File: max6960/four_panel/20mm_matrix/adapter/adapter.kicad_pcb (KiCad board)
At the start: 2 copper layers, 40 x 40 mm, 6 parts, among them M1 BETLUX-LED-8X8_C, M2 BETLUX-LED-8X8_C, M3 BETLUX-LED-8X8_C, M4 BETLUX-LED-8X8_C, P1 LED-MATRIX-2X-8X8-FEMALE, P2 LED-MATRIX-2X-8X8-FEMALE

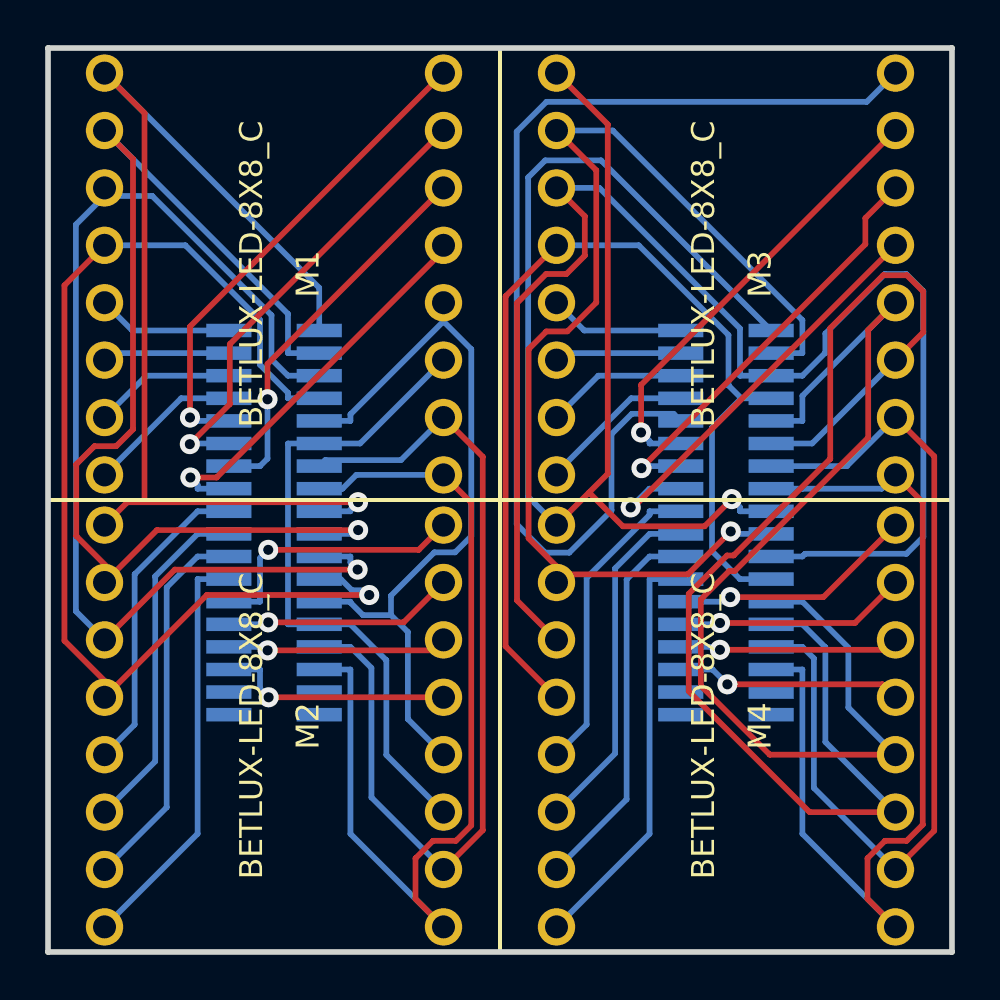
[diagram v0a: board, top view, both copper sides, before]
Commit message: Re-routed four matrix panel driver and adapter. Switched to board-to-board connectors from major league.
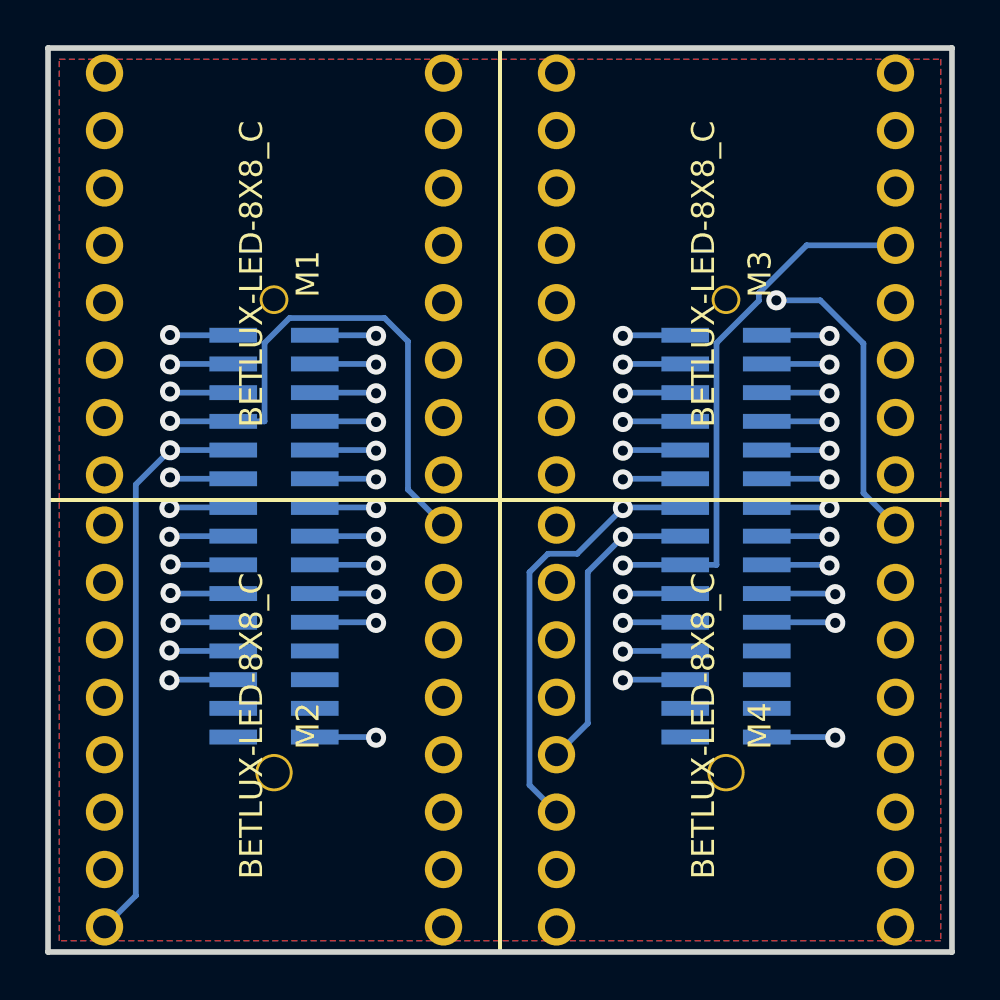
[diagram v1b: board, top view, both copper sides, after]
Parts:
- P1, P2: value LED-MATRIX-2X-8X8-FEMALE -> CONN15X2; footprint SMD_HEADER_18X2 -> SMD_PIN_ARRAY_F_0P5IN_15X2
- moved P1 0.60 mm to (60.0, 71.6)
- moved P2 0.60 mm to (80.0, 71.6)
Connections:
- P1 pad 1: /ROW_A1 -> /COL_A16
- P1 pad 10: /COL_A5 -> /ROW_A5
- P1 pad 11: /ROW_A6 -> /COL_A11
- P1 pad 12: /COL_A6 -> /ROW_A6
- P1 pad 13: /ROW_A7 -> /COL_A10
- P1 pad 14: /COL_A7 -> /ROW_A7
- P1 pad 15: /ROW_A8 -> /COL_A9
- P1 pad 16: /COL_A8 -> /ROW_A8
- P1 pad 17: /ROW_A1 -> /COL_A8
- P1 pad 18: /COL_A9 -> /COL_A1
- P1 pad 19: /ROW_A2 -> /COL_A7
- P1 pad 2: /COL_A1 -> /ROW_A1
- P1 pad 20: /COL_A10 -> /COL_A2
- P1 pad 21: /ROW_A3 -> /COL_A6
- P1 pad 22: /COL_A11 -> /COL_A3
- P1 pad 23: /ROW_A4 -> /COL_A5
- P1 pad 24: /COL_A12 -> N-0000035
- P1 pad 25: /ROW_A5 -> /COL_A4
- P1 pad 26: /COL_A13 -> N-0000036
- P1 pad 27: /ROW_A6 -> N-0000023
- P1 pad 28: /COL_A14 -> N-0000037
- P1 pad 29: /ROW_A7 -> N-0000022
- P1 pad 3: /ROW_A2 -> /COL_A15
- P1 pad 30: /COL_A15 -> GND
- P1 pad 4: /COL_A2 -> /ROW_A2
- P1 pad 5: /ROW_A3 -> /COL_A14
- P1 pad 6: /COL_A3 -> /ROW_A3
- P1 pad 7: /ROW_A4 -> /COL_A13
- P1 pad 8: /COL_A4 -> /ROW_A4
- P1 pad 9: /ROW_A5 -> /COL_A12
- P2 pad 1: /ROW_B1 -> /COL_B16
- P2 pad 10: /COL_B5 -> /ROW_B5
- P2 pad 11: /ROW_B6 -> /COL_B11
- P2 pad 12: /COL_B6 -> /ROW_B6
- P2 pad 13: /ROW_B7 -> /COL_B10
- P2 pad 14: /COL_B7 -> /ROW_B7
- P2 pad 15: /ROW_B8 -> /COL_B9
- P2 pad 16: /COL_B8 -> /ROW_B8
- P2 pad 17: /ROW_B1 -> /COL_B8
- P2 pad 18: /COL_B9 -> /COL_B1
- P2 pad 19: /ROW_B2 -> /COL_B7
- P2 pad 2: /COL_B1 -> /ROW_B1
- P2 pad 20: /COL_B10 -> /COL_B2
- P2 pad 21: /ROW_B3 -> /COL_B6
- P2 pad 22: /COL_B11 -> /COL_B3
- P2 pad 23: /ROW_B4 -> /COL_B5
- P2 pad 24: /COL_B12 -> N-0000031
- P2 pad 25: /ROW_B5 -> /COL_B4
- P2 pad 26: /COL_B13 -> N-0000029
- P2 pad 27: /ROW_B6 -> N-0000027
- P2 pad 28: /COL_B14 -> N-0000026
- P2 pad 29: /ROW_B7 -> N-0000024
- P2 pad 3: /ROW_B2 -> /COL_B15
- P2 pad 30: /COL_B15 -> GND
- P2 pad 4: /COL_B2 -> /ROW_B2
- P2 pad 5: /ROW_B3 -> /COL_B14
- P2 pad 6: /COL_B3 -> /ROW_B3
- P2 pad 7: /ROW_B4 -> /COL_B13
- P2 pad 8: /COL_B4 -> /ROW_B4
- P2 pad 9: /ROW_B5 -> /COL_B12
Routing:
- net /ROW_B6: track 57.6 -> 29.4 mm, vias 0 -> 1
- net /COL_B16: track 10.0 -> 35.5 mm
- net /ROW_B3: track 64.6 -> 39.6 mm, vias 0 -> 1
- net /ROW_B5: track 48.7 -> 27.8 mm, vias 0 -> 1
- net /COL_A14: track 10.3 -> 31.0 mm
- net /COL_B3: track 6.27 -> 26.4 mm, vias 0 -> 1
- net /COL_A3: track 6.27 -> 26.1 mm, vias 0 -> 1
- net /ROW_B1: track 61.5 -> 42.3 mm
- net /COL_A8: track 17.6 -> 36.4 mm
- net /COL_A16: track 10.5 -> 28.8 mm
- net /COL_B2: track 5.63 -> 23.9 mm, vias 0 -> 1
- net /COL_A2: track 5.63 -> 23.4 mm, vias 0 -> 1
- net /ROW_B8: track 42.8 -> 25.3 mm, vias 0 -> 1
- net /ROW_A8: track 42.9 -> 26.7 mm, vias 0 -> 1
- net /COL_B14: track 10.3 -> 26.3 mm
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- added copper zone on B.Cu, net GND
- added copper zone on F.Cu, net GND
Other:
- copper layers 2 -> 4
- net class Default: clearance 0.254 -> 0.2032
- rule trace_clearance: 0.254 -> 0.2032
